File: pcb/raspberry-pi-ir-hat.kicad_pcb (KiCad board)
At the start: 2 copper layers, 42.7 x 85 mm, 20 parts, among them J1 IO, J2 TX, J3 RX, J4 RX_JMP, J5 TX_JMP, J6 RW_JMP, J7 Raspberry_Pi_2_3, Q1 Q_NMOS_GSD

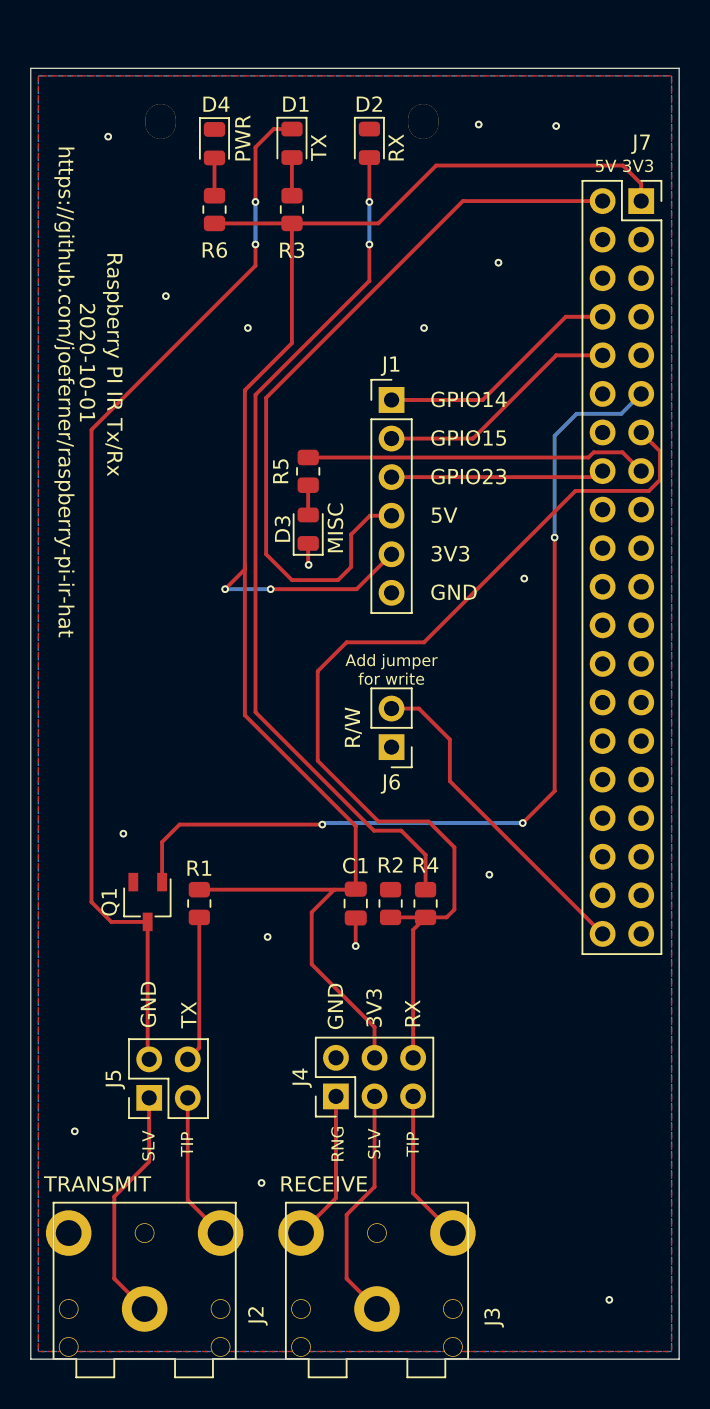
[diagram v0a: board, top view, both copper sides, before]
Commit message: cutout for ethernet port
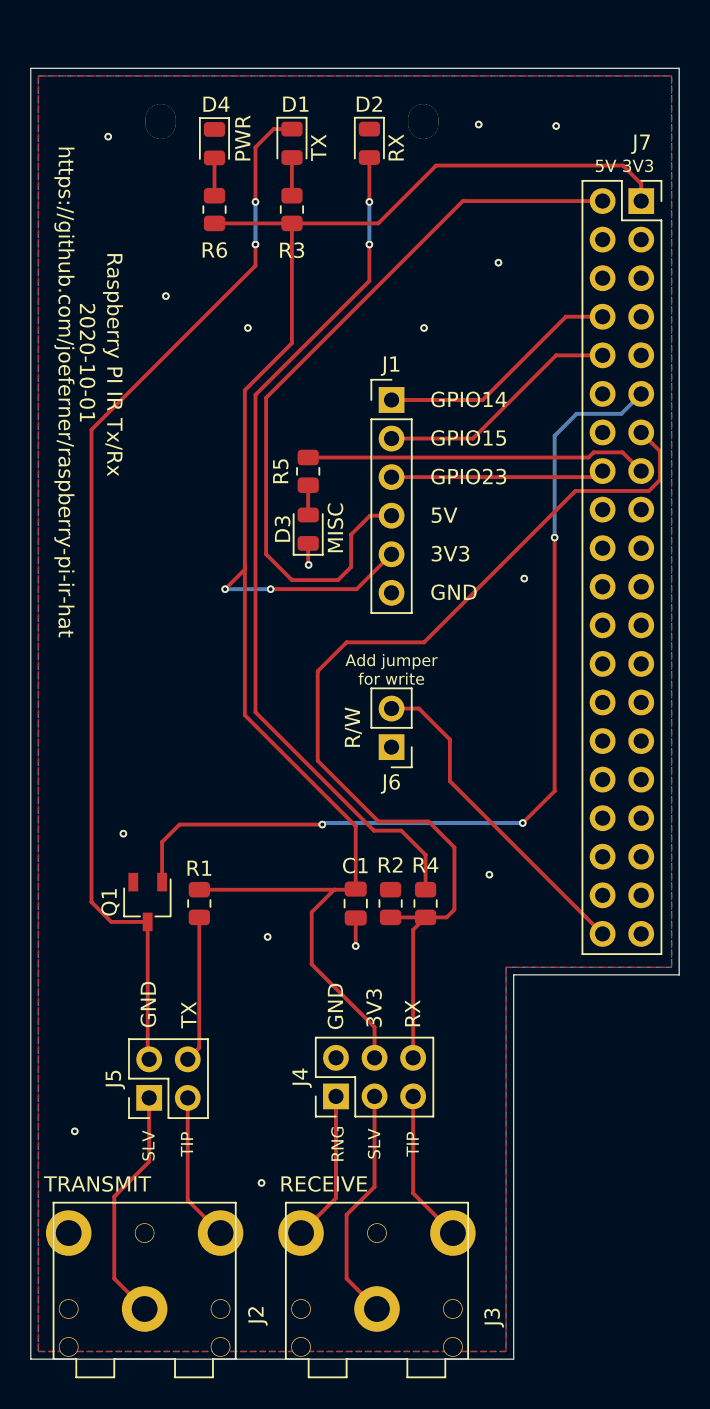
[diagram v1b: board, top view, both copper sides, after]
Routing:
- net GND: vias 16 -> 15
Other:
- outline, holes or cut-outs redrawn

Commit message: wip
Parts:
- added REF**: MountingHole_2.5mm_Pad, MountingHole:MountingHole_2.5mm_Pad, F.Cu at (135.5, 90.0)
- added REF**: MountingHole_2.5mm_Pad, MountingHole:MountingHole_2.5mm_Pad, F.Cu at (110.5, 146.0)
- moved J5 2.40 mm to (116.2, 143.7)
- moved J2 0.50 mm to (113.5, 157.2)
- moved J3 0.50 mm to (128.8, 157.2)
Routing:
- net VCC: track 117.2 -> 114.6 mm, vias 2 -> 4
- net Net-(J2-Pad2): track 9.79 -> 8.60 mm
- net Net-(J2-Pad1): track 15.7 -> 14.6 mm
- net Net-(D1-Pad1): track 70.4 -> 71.3 mm
- net Net-(J3-Pad1): track 15.6 -> 14.9 mm
- net Net-(J3-Pad3): track 9.95 -> 9.45 mm
- net Net-(J3-Pad2): track 10.1 -> 9.59 mm
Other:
- board size 42.7 x 85 mm -> 42.7 x 84.5 mm
